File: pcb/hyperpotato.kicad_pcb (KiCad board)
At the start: 2 copper layers, 121 x 101.8 mm, 53 parts, among them J1 Conn_01x02_Socket, J2 Conn_01x03_Pin, J3 Conn_01x05_Socket, Q1 AO3401A, SW1 SW_Push_45deg, SW10 SW_Push_45deg, SW11 SW_Push_45deg, SW12 SW_Push_45deg, SW13 SW_Push_45deg, SW14 SW_SPDT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

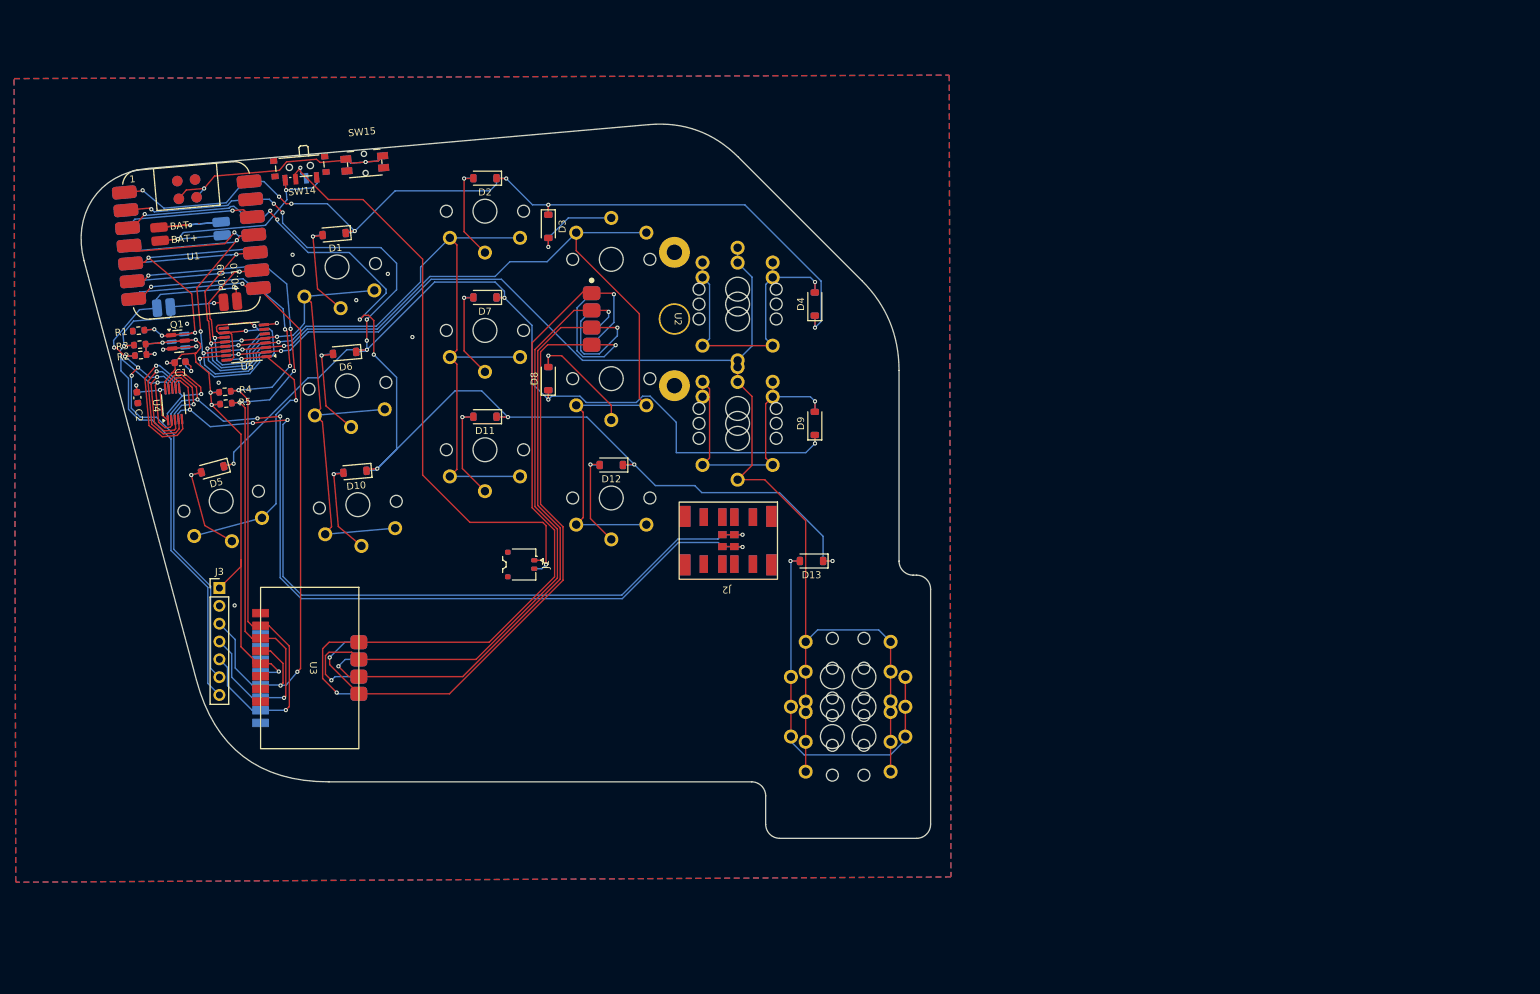
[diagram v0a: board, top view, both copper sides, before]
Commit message: Finish edge cuts
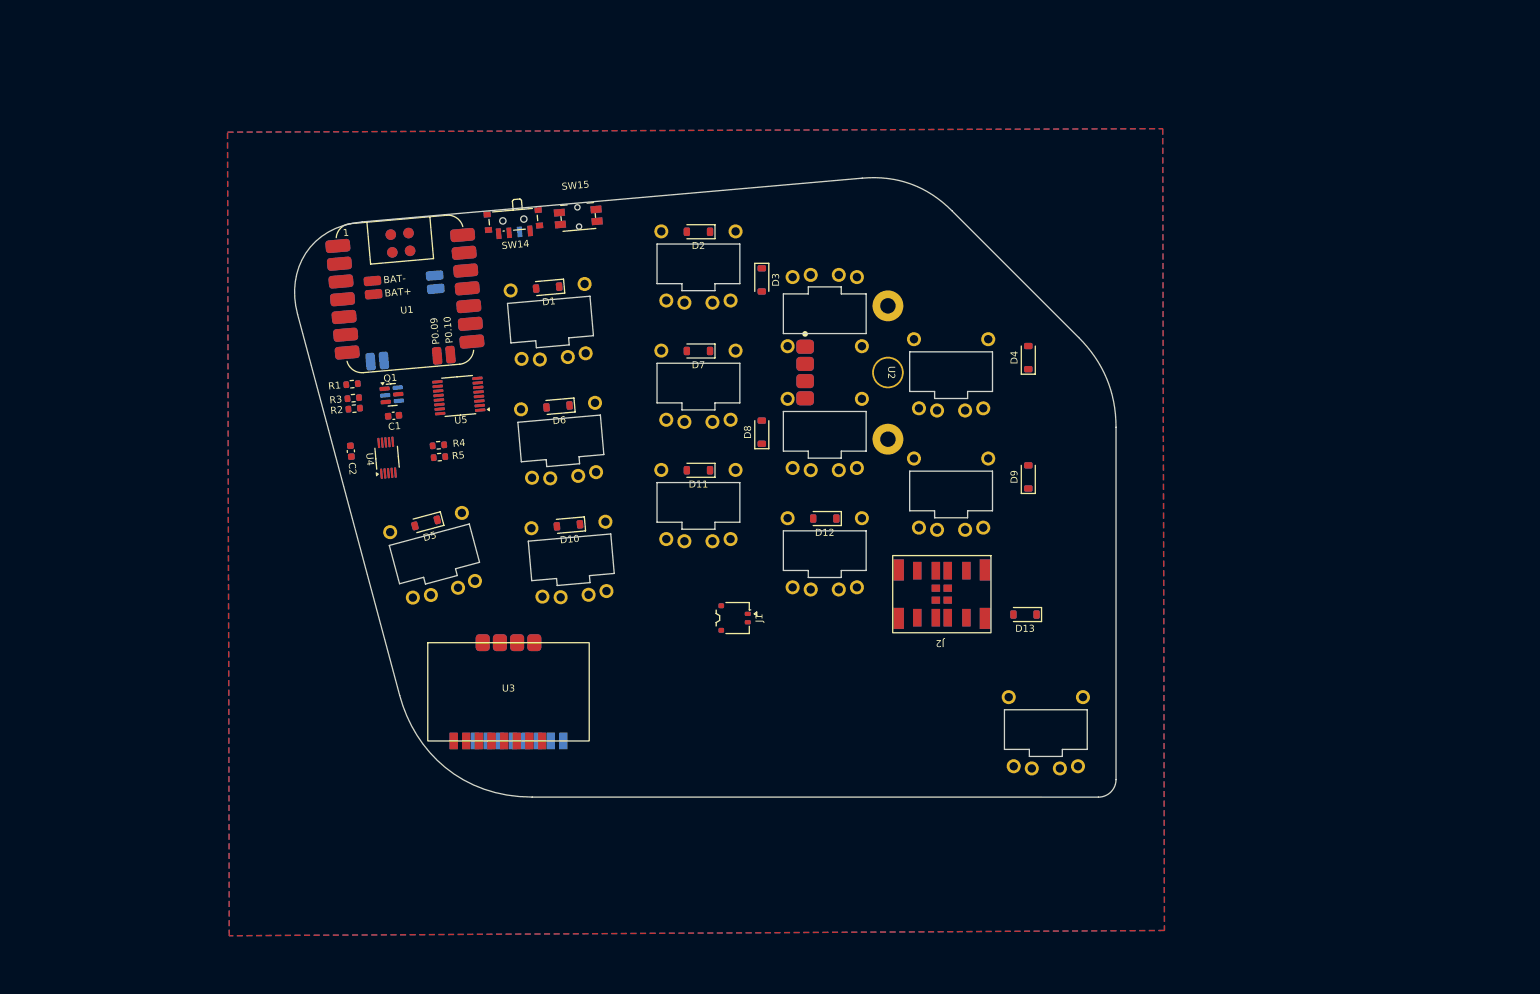
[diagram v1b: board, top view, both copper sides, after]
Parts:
- removed J3: Conn_01x05_Socket, Connector_PinHeader_2.54mm:PinHeader_1x07_P2.54mm_Vertical
- removed the SW13 at (161.6, 135.0)
- removed the SW13 at (161.6, 139.2)
- removed the SW13 at (166.1, 135.0)
- removed the SW13 at (166.1, 130.7)
- removed the SW13 at (166.1, 139.2)
- removed the SW4 at (148.1, 75.5)
- removed the SW4 at (148.1, 77.6)
- removed the SW9 at (148.1, 94.6)
- removed the SW9 at (148.1, 92.5)
- SW1, SW10, SW11, SW12, SW2, SW3, SW4, SW5, SW6, SW7, SW8, SW9: footprint ssbb_parts:SW_choc_v1_reversible_1u -> ssbb_parts:SW_Choc_Mini_reversible_1u
- SW13: footprint ssbb_parts:SW_choc_v1_reversible_1.5u -> ssbb_parts:SW_Choc_Mini_reversible_1u
- moved SW6 31.4 mm to (122.9, 96.9)
- moved D10 31.4 mm to (124.0, 109.1)
- moved C1 31.4 mm to (99.1, 93.5)
- moved R4 31.4 mm to (105.5, 97.7)
- moved SW2 31.4 mm to (142.5, 72.0)
- moved SW10 31.4 mm to (124.4, 113.8)
- moved D8 31.4 mm to (151.6, 95.9)
- moved SW3 31.4 mm to (160.5, 78.9)
- moved R5 31.4 mm to (105.6, 99.4)
- moved D2 31.4 mm to (142.5, 67.3)
- moved SW11 31.4 mm to (142.5, 106.0)
- moved J1 31.4 mm to (147.7, 122.4)
- moved D11 31.4 mm to (142.5, 101.3)
- moved SW14 31.4 mm to (116.2, 66.0)
- moved J2 31.4 mm to (177.2, 119.0)
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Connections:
- Q1 pad 2: +3V3 -> +3.3V
- U5 pad 10: VCC -> +3.3V
- U5 pad 16: VCC -> +3.3V
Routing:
- net COL4: track 198.3 -> 0.00 mm, vias 2 -> 0
- net ROW1: track 185.2 -> 0.00 mm, vias 10 -> 0
- net ROW2: track 166.1 -> 0.00 mm, vias 9 -> 0
- net COL3: track 133.2 -> 0.00 mm, vias 2 -> 0
- net +3.3V_OPTIONAL: track 131.6 -> 0.00 mm, vias 9 -> 0
- net ROW0: track 130.6 -> 0.00 mm, vias 7 -> 0
- net Net-(J2-Pin_1): track 122.8 -> 0.00 mm, vias 4 -> 0
- net Net-(J2-Pin_2): track 119.4 -> 0.00 mm, vias 4 -> 0
- net TP_S4: track 108.4 -> 0.00 mm, vias 2 -> 0
- net TP_CLK: track 108.3 -> 0.00 mm, vias 5 -> 0
- net TP_DATA: track 105.5 -> 0.00 mm, vias 5 -> 0
- net COL2: track 105.1 -> 0.00 mm, vias 2 -> 0
- net TP_S1: track 105.0 -> 0.00 mm, vias 2 -> 0
- net TP_S3: track 101.9 -> 0.00 mm, vias 2 -> 0
- net SDA: track 100.8 -> 0.00 mm, vias 6 -> 0
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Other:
- board size 121 x 101.8 mm -> 117 x 88.3 mm

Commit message: Got good arrangement
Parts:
- added J3: Conn_01x05_Socket, Connector_PinHeader_2.54mm:PinHeader_1x07_P2.54mm_Vertical, F.Cu at (236.0, 94.6)
- added TP1: , hyperpotato:trackpoint_mount_t430, F.Cu at (169.5, 87.4)
- D1, D10, D11, D12, D13, D2, D3, D4, D5, D6, D7, D8, D9: footprint ssbb_parts:D_SOD-123_reversible -> Diode_SMD:D_1206_3216Metric
- moved U2 53.6 mm to (221.5, 100.4), turned to 0 degrees
- moved J1 30.4 mm to (177.7, 117.6)
- moved J2 15.0 mm to (192.0, 121.4)
- moved D13 13.9 mm to (195.3, 109.4)
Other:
- outline, holes or cut-outs redrawn

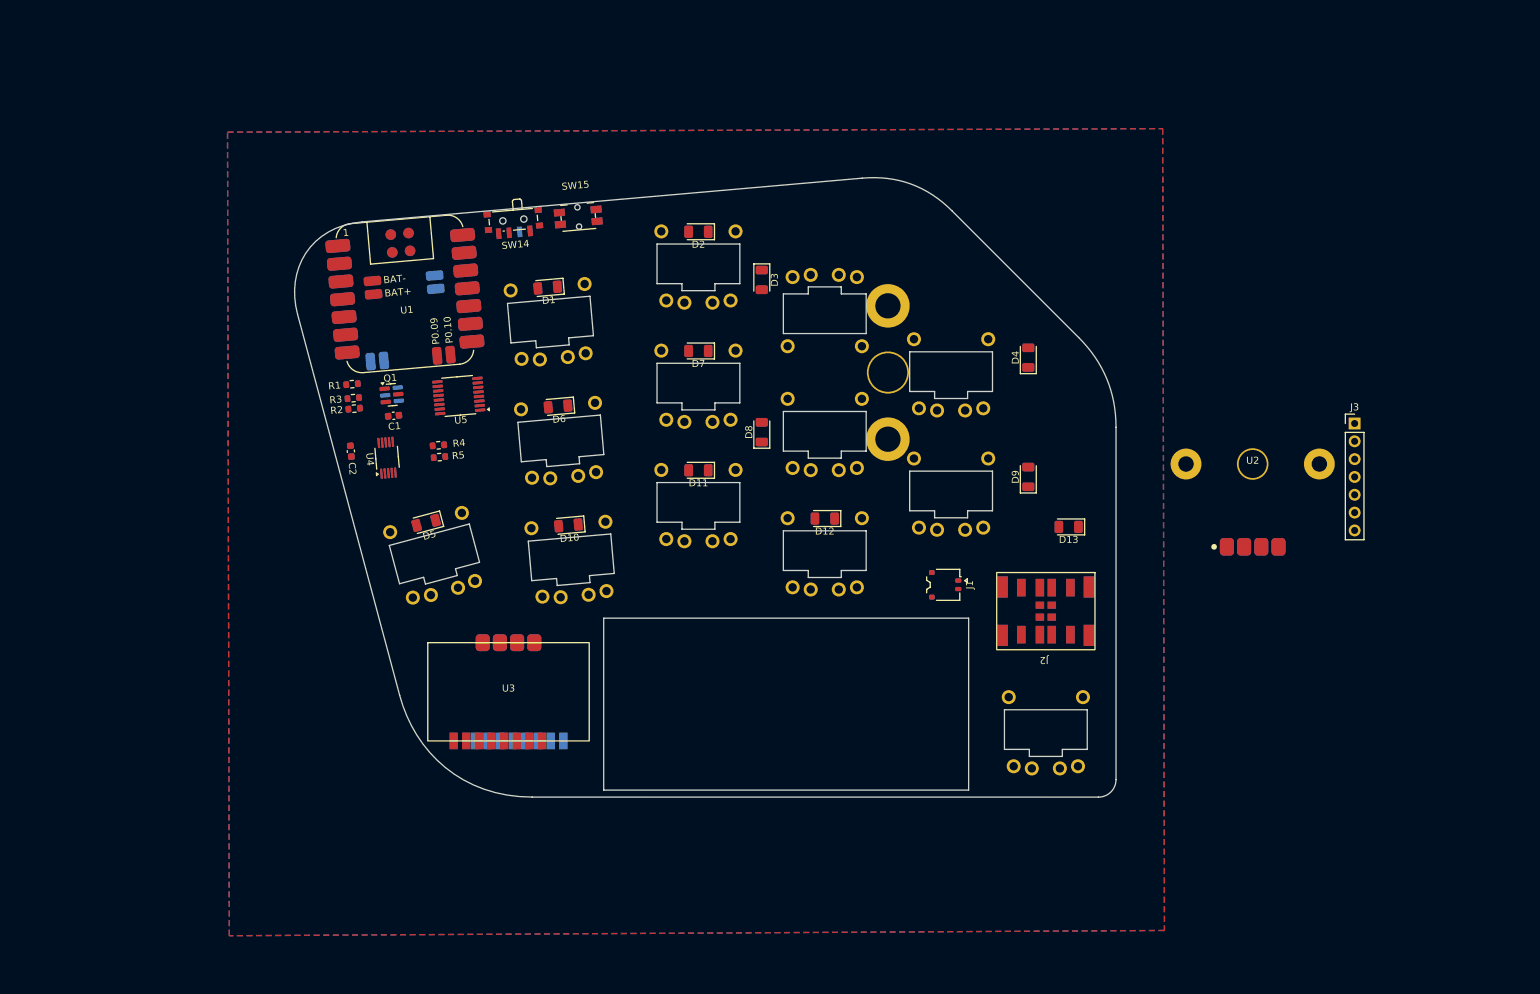
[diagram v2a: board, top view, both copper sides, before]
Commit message: Basic routing and diodes routing
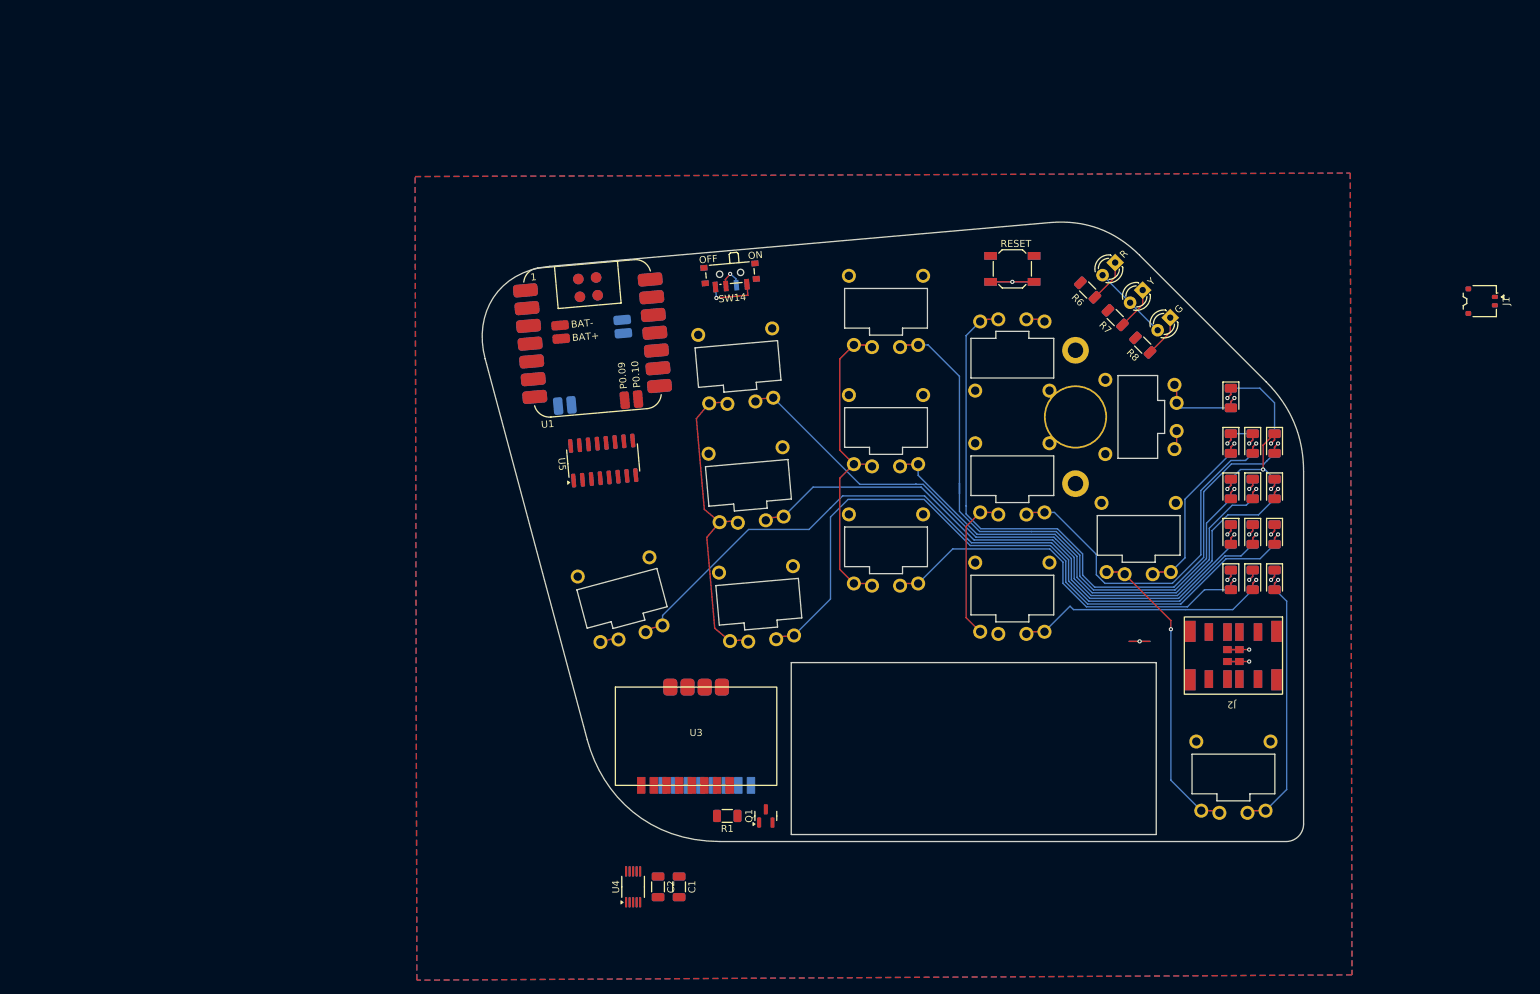
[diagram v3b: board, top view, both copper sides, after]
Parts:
- removed J3: Conn_01x05_Socket, Connector_PinHeader_2.54mm:PinHeader_1x07_P2.54mm_Vertical
- removed R2, R3, R4, R5: R_Small, ssbb_parts:R_0603_1608Metric_reversible
- removed the U2 at (221.5, 100.4)
- added D14: R, LED_THT:LED_D3.0mm, F.Cu at (201.9, 71.7)
- added D15: Y, LED_THT:LED_D3.0mm, F.Cu at (205.8, 75.6)
- added D16: G, LED_THT:LED_D3.0mm, F.Cu at (209.8, 79.5)
- added R6: 220, ssbb_parts_reversible:R_1206_3216Metric_reversible, F.Cu at (198.0, 75.6)
- added R7: 220, ssbb_parts_reversible:R_1206_3216Metric_reversible, F.Cu at (201.9, 79.5)
- added R8: 220, ssbb_parts_reversible:R_1206_3216Metric_reversible, F.Cu at (205.8, 83.5)
- C1, C2: footprint ssbb_parts:C_0603_1608Metric_reversible -> ssbb_parts_reversible:C_1206_3216Metric_reversible
- D1, D10, D11, D12, D13, D2, D3, D4, D5, D6, D7, D8: footprint Diode_SMD:D_1206_3216Metric -> ssbb_parts_reversible:D_1206_3216Metric_reversible
- D9: footprint Diode_SMD:D_1206_3216Metric -> ssbb_parts_reversible:D_1206_3216Metric_reversible; moved to B.Cu
- J1: footprint ssbb_parts:Molex_Pico-EZmate_78171-0002_1x02-1MP_P1.20mm_Vertical_reversible -> ssbb_parts_reversible:Molex_Pico-EZmate_78171-0002_1x02-1MP_P1.20mm_Vertical_reversible
- Q1: footprint ssbb_parts:SOT-23_reversible -> Package_TO_SOT_SMD:SOT-23
- R1: footprint ssbb_parts:R_0603_1608Metric_reversible -> ssbb_parts_reversible:R_1206_3216Metric_reversible
- SW14: footprint ssbb_parts:SW_SPDT_PCM12_reversible -> ssbb_parts_reversible:SW_SPDT_PCM12_reversible
- SW15: footprint ssbb_parts:Panasonic_EVQPUL_EVQPUC_reversible -> ssbb_parts:SW_SPST_SKQG_WithStem_reversible
- U2: renamed from TP1; value (none) -> SK8707-01-SENSOR; footprint hyperpotato:trackpoint_mount_t430 -> ssbb_parts:TP_Lenovo_T460S_Sensor
- U3: footprint ssbb_parts:Sprintek_SK8707-01_reversible -> ssbb_parts:TP_Sprintek_SK8707-01_reversible
- U4: footprint ssbb_parts:VSSOP-10_3x3mm_P0.5mm_reversible -> ssbb_parts_reversible:VSSOP-10_3x3mm_P0.5mm_reversible
- U5: footprint ssbb_parts:TSSOP-16_4.4x5mm_P0.65mm_reversible -> ssbb_parts_reversible:SOIC-16_3.9x9.9mm_P1.27mm_reversible
- moved D5 117.8 mm to (221.5, 110.4), turned to -90 degrees
- moved D1 107.5 mm to (224.6, 104.0), turned to -90 degrees
- moved D10 100.6 mm to (224.6, 110.4), turned to -90 degrees
- moved D6 97.6 mm to (218.4, 110.4), turned to -90 degrees
- moved J1 86.5 mm to (254.1, 77.2)
- moved D2 84.3 mm to (218.4, 104.0), turned to -90 degrees
- moved R1 81.5 mm to (146.6, 150.5), turned to 180 degrees
- moved D7 81.4 mm to (221.5, 104.0), turned to -90 degrees
- moved Q1 80.3 mm to (152.1, 150.5), turned to 90 degrees
- moved C1 78.5 mm to (139.8, 160.6), turned to -90 degrees
- moved D11 77.5 mm to (218.4, 116.9), turned to -90 degrees
- moved D3 76.7 mm to (224.6, 97.5)
- moved C2 75.9 mm to (136.8, 160.6), turned to -90 degrees
- moved U4 70.5 mm to (133.2, 160.6), turned to 90 degrees
- moved D8 70.0 mm to (221.5, 97.5), turned to -90 degrees
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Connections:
- C1 pad 1: +3.3V_OPTIONAL -> +3.3V
- SW14 pad 1: unconnected-(SW14-A-Pad1)_1 -> +BATT
- SW14 pad 3: BAT+ -> unconnected-(SW14-C-Pad3)_1
- SW4 pad 1: Net-(D4-A) -> COL4
- SW4 pad 2: COL4 -> Net-(D4-A)
- SW6 pad 1: COL1 -> unconnected-(SW6-Pad1)
- SW9 pad 1: Net-(D9-A) -> unconnected-(SW9-Pad1)
- SW9 pad 2: COL4 -> Net-(D9-A)
- U1 pad 16: BAT+ -> +BATT
- U1 pad 5: POWER_CUTOFF -> TP_CLK
- U1 pad 6: TP_CLK -> TP_DATA
- U1 pad 7: TP_DATA -> POWER_CUTOFF
- U3 pad 5: +3.3V_OPTIONAL -> +3.3V
- U4 pad 10: +3.3V_OPTIONAL -> +3.3V
- U4 pad 5: +3.3V_OPTIONAL -> +3.3V
- U5 pad 15: unconnected-(U5-QA-Pad15) -> LED1
- U5 pad 6: unconnected-(U5-QG-Pad6) -> LED2
- U5 pad 7: unconnected-(U5-QH-Pad7)_1 -> LED3
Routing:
- net Net-(D5-A): track 0.00 -> 109.9 mm, vias 0 -> 1
- net Net-(D10-A): track 0.00 -> 100.7 mm, vias 0 -> 1
- net Net-(D1-A): track 0.00 -> 99.2 mm, vias 0 -> 1
- net Net-(D3-A): track 0.00 -> 97.7 mm, vias 0 -> 1
- net Net-(D2-A): track 0.00 -> 87.9 mm, vias 0 -> 1
- net Net-(D6-A): track 0.00 -> 83.1 mm, vias 0 -> 1
- net Net-(D7-A): track 0.00 -> 72.1 mm, vias 0 -> 1
- net Net-(D11-A): track 0.00 -> 58.7 mm, vias 0 -> 1
- net Net-(D8-A): track 0.00 -> 54.5 mm, vias 0 -> 1
- net COL4: track 0.00 -> 46.3 mm, vias 0 -> 1
- net COL1: track 0.00 -> 45.5 mm
- net COL2: track 0.00 -> 45.4 mm
- net Net-(D13-A): track 0.00 -> 39.4 mm, vias 0 -> 1
- net Net-(D12-A): track 0.00 -> 38.5 mm, vias 0 -> 1
- net ROW0: track 0.00 -> 37.5 mm, vias 0 -> 5
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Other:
- board text added: "Diodes are placed like to be solder together with a haptics module in one go."
- board text added: "OFF"
- board text added: "ON"
- board text added: "RESET"
- board text added: "Trackpoint is going to be mounted on the right side, and the switch pin won't collide with it in this orientation."
- board text removed: "3mm offset"
- board text removed: "A few reasons to place diodes like this: - Aesthetics - The trackpoint sensor PCB would collide with them when placed in a LED hole - They are easy to solder with a hot plate this way"
- board text removed: "Trackpoint is going to be mounted on the right side, and the switch pin won't collide with it in this orientation. Will need to cut stab pins though."

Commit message: Good progsess on tracks
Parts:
- added U2: SK8707-01-SENSOR, ssbb_parts:TP_Sensor_Connector_reversible, F.Cu at (181.6, 81.3)
- H1: renamed from U2; value SK8707-01-SENSOR -> MountingHole
- moved J1 59.3 mm to (205.4, 111.1), turned to 90 degrees
- moved SW7 12.9 mm to (172.6, 82.9)
- moved SW8 12.9 mm to (190.6, 89.8)
- moved D2 12.9 mm to (221.8, 91.6)
- moved SW3 12.9 mm to (190.6, 72.8)
- moved D6 12.9 mm to (221.8, 98.0)
- moved D8 12.9 mm to (224.9, 85.1)
- moved R8 12.9 mm to (209.2, 71.1)
- moved SW2 12.9 mm to (172.6, 65.9)
- moved SW5 12.9 mm to (135.1, 107.3)
- moved SW6 12.9 mm to (153.0, 90.8)
- moved D15 12.9 mm to (209.2, 63.2)
- moved SW15 12.9 mm to (190.6, 60.2)
- moved C1 12.9 mm to (143.2, 148.3)
- moved D11 12.9 mm to (221.8, 104.5)
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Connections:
- H1 pad 1: TP_S1 -> (no net)
- SW6 pad 1: unconnected-(SW6-Pad1) -> COL1
- SW9 pad 1: unconnected-(SW9-Pad1) -> COL4
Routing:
- net COL4: track 46.3 -> 168.9 mm, vias 1 -> 0
- net ROW2: track 12.9 -> 112.8 mm, vias 4 -> 5
- net ROW1: track 19.2 -> 117.7 mm, vias 5 -> 7
- net TP_S1: track 0.00 -> 83.6 mm, vias 0 -> 1
- net TP_S2: track 0.00 -> 82.0 mm, vias 0 -> 1
- net TP_S3: track 0.00 -> 79.5 mm, vias 0 -> 1
- net TP_S4: track 0.00 -> 75.9 mm, vias 0 -> 1
- net ROW0: track 37.5 -> 111.7 mm
- net LED3: track 0.00 -> 55.6 mm, vias 0 -> 1
- net COL3: track 24.1 -> 77.3 mm
- net LED2: track 0.00 -> 51.2 mm, vias 0 -> 1
- net LED1: track 0.00 -> 47.1 mm, vias 0 -> 1
- net RESET: track 12.4 -> 43.2 mm
- net COL2: track 45.4 -> 69.4 mm
- net Net-(D5-A): track 109.9 -> 118.3 mm
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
